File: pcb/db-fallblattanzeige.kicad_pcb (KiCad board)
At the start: 2 copper layers, 50 x 50 mm, 21 parts, among them IC1 ATMEGA328-P, IC2 MAX485, P1 2x9_pin_holes, P2 FTDI_header, Y1 Crystal

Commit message: corrected zilog footprint and silk
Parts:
- P1: value 2x9_pin_holes -> ZiLOG_3562_FBM_V2.02; footprint Socket_Strips:Socket_Strip_Straight_2x09 -> c-base-db:ZiLOG_3562_FBM_V2.02
- moved P1 20.2 mm to (188.0, 78.2), turned to 0 degrees
- moved P2 13.0 mm to (168.2, 109.4), turned to 0 degrees
- moved Power Select 4.42 mm to (183.6, 122.6), turned to 90 degrees
- moved G*** 0.91 mm to (206.6, 114.4)
- moved Debug Override 0.18 mm to (174.2, 122.6)
- renumbered 100nF1 to 100nF, 100nF2 to 100nF, 100nF3 to 100nF
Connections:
- 100nF pad 1: VCC -> Net-(100nF1-Pad1)
- 100nF pad 1: Net-(100nF3-Pad1) -> VCC
- IC1 pad 12: //SR_LATCH -> /~SR_LATCH
- IC1 pad 21: Net-(100nF3-Pad1) -> Net-(100nF1-Pad1)
- P1 pad 10: GND -> (no net)
- P1 pad 11: (no net) -> /BUS_MINUS
- P1 pad 12: /PWR_IR2 -> /PWR_IR1
- P1 pad 13: (no net) -> /PWR_IR2
- P1 pad 14: /PWR_IR1 -> GND
- P1 pad 15: /IR_IN -> /SCL
- P1 pad 16: /BUS_MINUS -> /SDA
- P1 pad 17: /BUS_PLUS -> /Motor
- P1 pad 18: (no net) -> /~SR_LATCH
- P1 pad 2: //SR_LATCH -> /SR_CP
- P1 pad 3: /SR_CP -> (no net)
- P1 pad 4: /Motor -> (no net)
- P1 pad 5: (no net) -> +5VD
- P1 pad 6: /SDA -> (no net)
- P1 pad 8: /SCL -> /IR_IN
- P1 pad 9: +5VD -> /BUS_PLUS
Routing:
- net Net-(IC1-Pad3): track 77.1 -> 0.00 mm, vias 2 -> 0
- net +5VD: track 68.9 -> 0.00 mm
- net /IR_IN: track 34.4 -> 0.00 mm, vias 2 -> 0
- net Net-(C3-Pad1): track 31.5 -> 2.54 mm
- net /SR_DATA: track 28.2 -> 0.64 mm, vias 1 -> 0
- net /SR_CP: track 26.3 -> 0.00 mm, vias 1 -> 0
- net Net-(JP2-Pad3): track 22.9 -> 0.06 mm
- net //SR_LATCH: track 22.2 -> 0.00 mm, vias 1 -> 0
- net /Motor: track 21.9 -> 0.00 mm, vias 3 -> 0
- net /SDA: track 19.6 -> 0.00 mm
- net VCC: track 121.3 -> 102.3 mm, vias 4 -> 2
- net +5VA: track 19.1 -> 2.29 mm
- net /SCL: track 17.7 -> 3.23 mm, vias 1 -> 0
- net /PWR_IR1: track 10.2 -> 0.51 mm, vias 1 -> 0
- net GND: track 100.3 -> 108.3 mm
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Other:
- board text added: "CTS RX TX VCC CTS GND"
- board text removed: "RTS RX TX VCC CTS GND"

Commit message: finished revision 1
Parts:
- JP1: renamed from Power Select; value TX_SEL -> Debug Override
- JP2: renamed from Debug Override; value PWR_SEL -> Power Select
- moved C2 2.22 mm to (166.4, 102.1), turned to 270 degrees
- moved C1 1.59 mm to (166.4, 100.2), turned to 90 degrees
- moved D1 0.96 mm to (193.9, 118.5), turned to 0 degrees
- moved G*** 0.56 mm to (206.7, 115.0)
- turned Y1 to 270 degrees
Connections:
- JP1 pad 1: (no net) -> Net-(JP1-Pad1)
- JP1 pad 3: Net-(JP2-Pad3) -> (no net)
- P2 pad 3: Net-(JP2-Pad3) -> Net-(JP1-Pad1)
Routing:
- net GND: track 108.3 -> 0.44 mm, vias 1 -> 0
- net Net-(IC1-Pad3): track 0.00 -> 54.6 mm
- net /~SR_LATCH: track 0.00 -> 46.8 mm, vias 0 -> 2
- net /SR_DATA: track 0.64 -> 47.2 mm, vias 0 -> 1
- net /Motor: track 0.00 -> 44.3 mm, vias 0 -> 3
- net /SR_CP: track 0.00 -> 38.9 mm, vias 0 -> 3
- net +5VD: track 0.00 -> 38.5 mm
- net /BUS_PLUS: track 34.8 -> 56.6 mm, vias 0 -> 3
- net /IR_IN: track 0.00 -> 19.0 mm
- net Net-(JP1-Pad1): track 0.00 -> 18.9 mm
- net Net-(IC1-Pad2): track 74.2 -> 90.7 mm, vias 3 -> 4
- net /PWR_IR1: track 0.51 -> 16.8 mm
- net /SDA: track 0.00 -> 16.2 mm
- net VCC: track 102.3 -> 117.4 mm, vias 2 -> 3
- net Net-(C3-Pad1): track 2.54 -> 16.0 mm
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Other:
- board text added: "coon@c-base.org 04/2016"
- board text removed: "coon@c-base.org 03/2016"

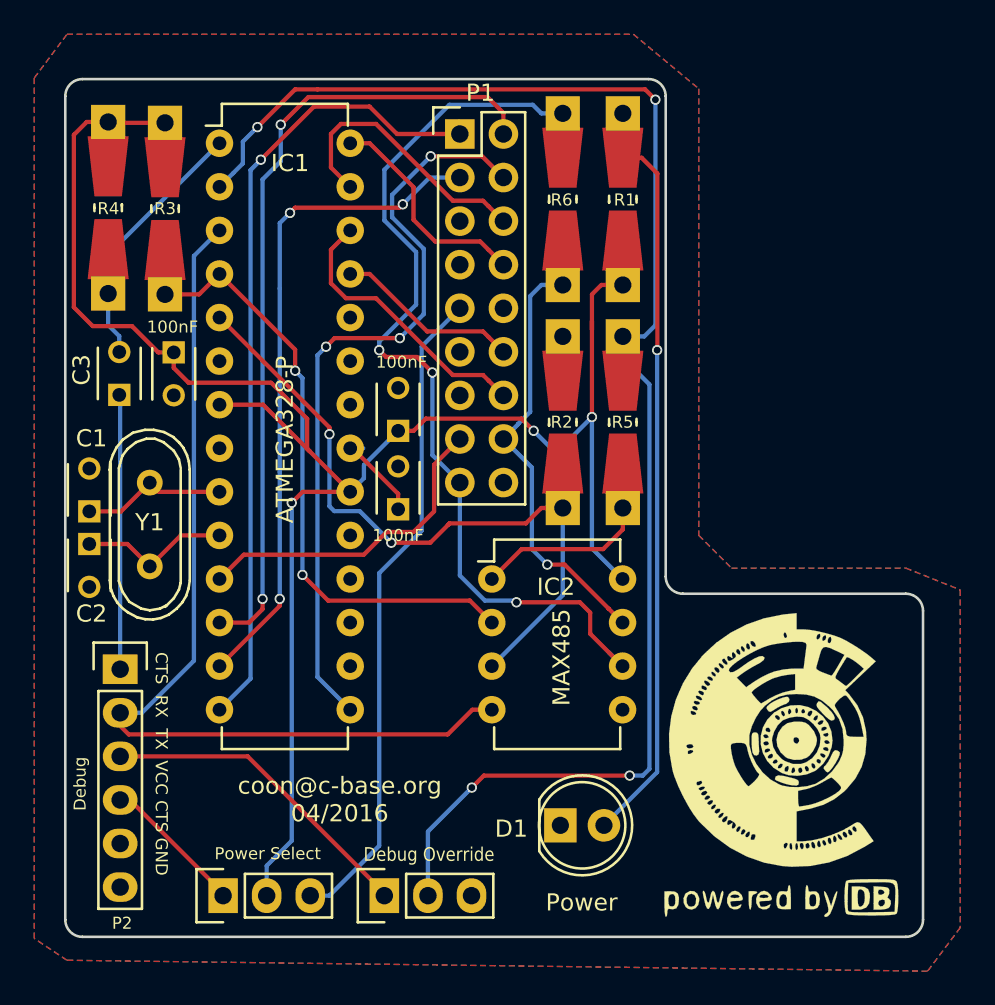
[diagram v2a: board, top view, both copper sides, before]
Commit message: fix 180° bug + R3/R4 swap (Rev2)
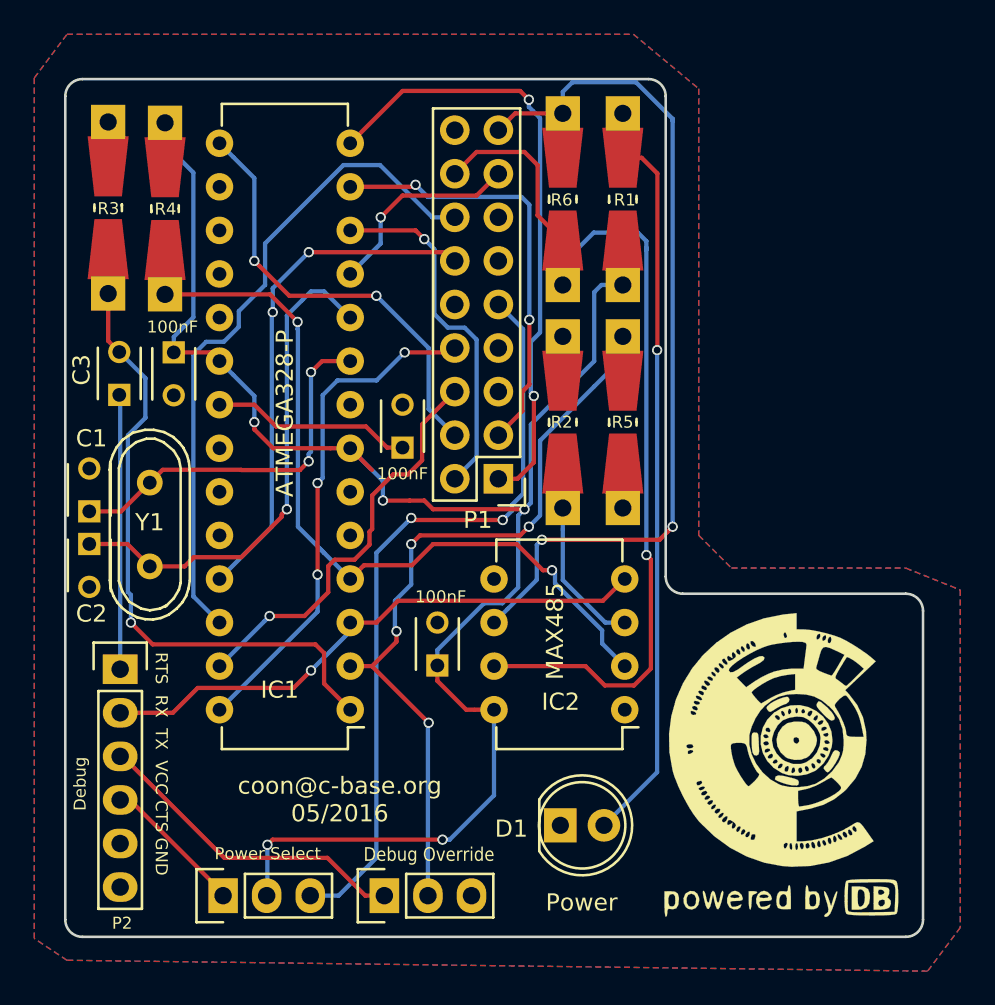
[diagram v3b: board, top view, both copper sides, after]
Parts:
- moved IC1 33.9 mm to (181.6, 111.8), turned to 180 degrees
- moved P1 20.2 mm to (190.2, 98.3), turned to 180 degrees
- moved 100nF 13.9 mm to (186.7, 109.2)
- moved IC2 10.9 mm to (197.6, 111.8), turned to 180 degrees
- moved 100nF 3.60 mm to (184.7, 96.5)
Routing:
- net Net-(IC1-Pad2): track 90.7 -> 47.2 mm
- net Net-(IC1-Pad5): track 42.6 -> 11.4 mm, vias 2 -> 0
- net /BUS_MINUS: track 27.9 -> 56.4 mm
- net /~SR_LATCH: track 46.8 -> 20.9 mm, vias 2 -> 1
- net /PWR_IR1: track 16.8 -> 39.3 mm
- net Net-(IC1-Pad3): track 54.6 -> 32.9 mm, vias 0 -> 1
- net Net-(C3-Pad2): track 17.7 -> 39.1 mm, vias 0 -> 1
- net Net-(C2-Pad1): track 8.88 -> 29.7 mm, vias 0 -> 1
- net /PWR_IR2: track 10.9 -> 29.9 mm, vias 0 -> 2
- net /Motor: track 44.3 -> 25.7 mm, vias 3 -> 2
- net /SCL: track 13.0 -> 29.7 mm, vias 0 -> 3
- net /SR_CP: track 38.9 -> 25.2 mm, vias 3 -> 2
- net Net-(C1-Pad1): track 8.51 -> 21.8 mm, vias 0 -> 2
- net VCC: track 117.4 -> 105.4 mm, vias 3 -> 5
- net /SR_DATA: track 47.2 -> 36.1 mm, vias 1 -> 2
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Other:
- board text added: "RTS RX TX VCC CTS GND"
- board text added: "coon@c-base.org 05/2016"
- board text removed: "CTS RX TX VCC CTS GND"
- board text removed: "coon@c-base.org 04/2016"
